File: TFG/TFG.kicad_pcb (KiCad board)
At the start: 2 copper layers, 68.3 x 67.9 mm, 36 parts, among them IC1 MC74VHC1GT14DBVT1G, IC2 AMS1117-5.0, IC3 AMS1117-5.0, J1 Jack-DC, J2 CON-SMA-EDGE-SRP, J3 CON-SMA-EDGE-SRP, Q1 BFP420

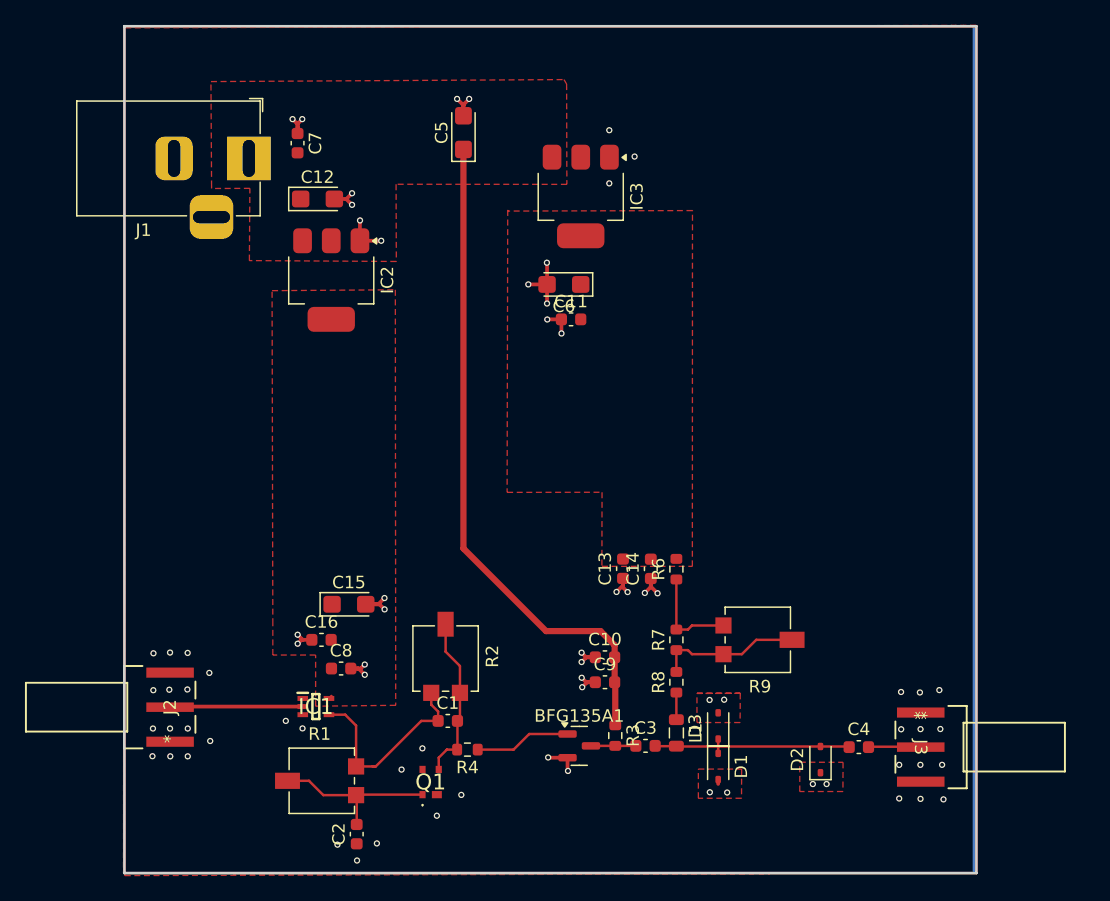
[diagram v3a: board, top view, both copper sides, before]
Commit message: Updated Schottky and SRD diodes in PCB and BOM, everything is ready to check, only DRC is missing
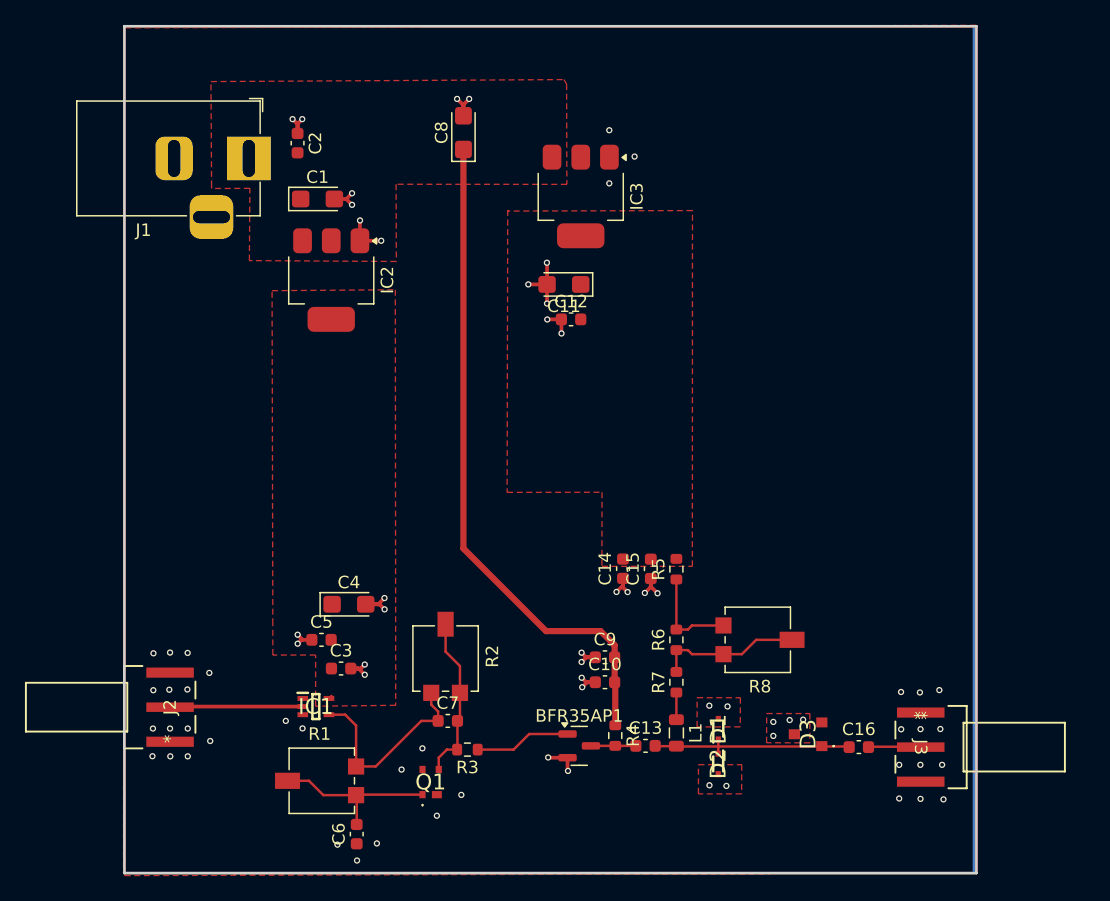
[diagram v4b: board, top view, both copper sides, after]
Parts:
- removed the D2 at (91.7, 75.4)
- added D3: SRD_MA144769-287T, MA144769-287T:MA144769287T, F.Cu at (90.7, 73.4)
- D1: renamed from D3; value D_Schottky_BAT15 -> SMS3923-079LF; footprint Diode_SMD:D_SOD-323 -> SMS3923-079LF:SODFL1608X70N
- D2: renamed from D1; value D_Schottky_BAT15 -> SMS3923-079LF; footprint Diode_SMD:D_SOD-323 -> SMS3923-079LF:SODFL1608X70N
- IC1: value MC74VHC1GT14DBVT1G -> MC74VHC1GT04DFT2G
- IC2, IC3: value AMS1117-5.0 -> TS1117BCW50 RPG
- moved D1 0.27 mm to (83.5, 73.0)
- moved D2 0.20 mm to (83.5, 75.7)
- renumbered BFG135A1 to BFR35AP1, C12 to C1, C9 to C10, C6 to C11, C11 to C12, C3 to C13, C13 to C14, C14 to C15, C4 to C16, C7 to C2, C8 to C3, C15 to C4, C16 to C5, C2 to C6, C1 to C7, C5 to C8, C10 to C9, R4 to R3, R3 to R4, R6 to R5, R7 to R6, R8 to R7, R9 to R8
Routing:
- net GND: track 38.1 -> 37.7 mm, vias 73 -> 75

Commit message: Final design for Ultrawideband pulse generator PCB - v1
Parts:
- added REF**: MountingHole_2mm, MountingHole:MountingHole_2mm, F.Cu at (50.9, 75.8)
- added REF**: MountingHole_2mm, MountingHole:MountingHole_2mm, F.Cu at (50.9, 34.1)
- added REF**: MountingHole_2mm, MountingHole:MountingHole_2mm, F.Cu at (99.6, 34.1)
- added REF**: MountingHole_2mm, MountingHole:MountingHole_2mm, F.Cu at (99.6, 75.8)
- moved C8 28.5 mm to (65.5, 53.5), turned to -90 degrees
- moved C2 21.0 mm to (61.3, 43.6), turned to 180 degrees
- moved C1 20.2 mm to (61.2, 48.1)
- moved IC3 19.5 mm to (74.0, 49.7), turned to 0 degrees
- moved J1 18.2 mm to (55.9, 42.4)
- moved IC2 17.9 mm to (56.7, 54.3), turned to 180 degrees
- moved C6 17.4 mm to (69.5, 72.5)
- moved C11 16.9 mm to (81.1, 51.0), turned to -90 degrees
- moved C12 16.0 mm to (83.9, 50.5), turned to 90 degrees
- moved C14 15.5 mm to (89.2, 52.2), turned to 180 degrees
- moved C15 15.0 mm to (89.2, 50.0), turned to 180 degrees
- moved R1 14.6 mm to (65.5, 72.5), turned to 90 degrees
- moved Q1 14.0 mm to (71.0, 68.0)
- moved R3 13.6 mm to (72.5, 64.5)
- moved J2 10.1 mm to (47.9, 66.8)
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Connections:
- J1 pad 3: (no net) -> GND
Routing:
- net /V12v: track 54.0 -> 0.57 mm
- net GND: track 37.7 -> 0.32 mm, vias 75 -> 116
- net Net-(IC1-Y): track 16.4 -> 9.75 mm
- net Net-(BFR35AP1-B): track 7.57 -> 4.04 mm
- net Net-(Q1-C): track 13.5 -> 16.2 mm
- net /Vout: track 5.46 -> 3.08 mm
- net Net-(R5-Pad1): track 7.95 -> 6.44 mm
- net /V3v_in: track 10.5 -> 9.27 mm
- net /V5v: track 1.05 -> 0.00 mm
- net Net-(Q1-B): track 13.7 -> 12.8 mm
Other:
- board size 68.3 x 67.9 mm -> 56.7 x 48.9 mm

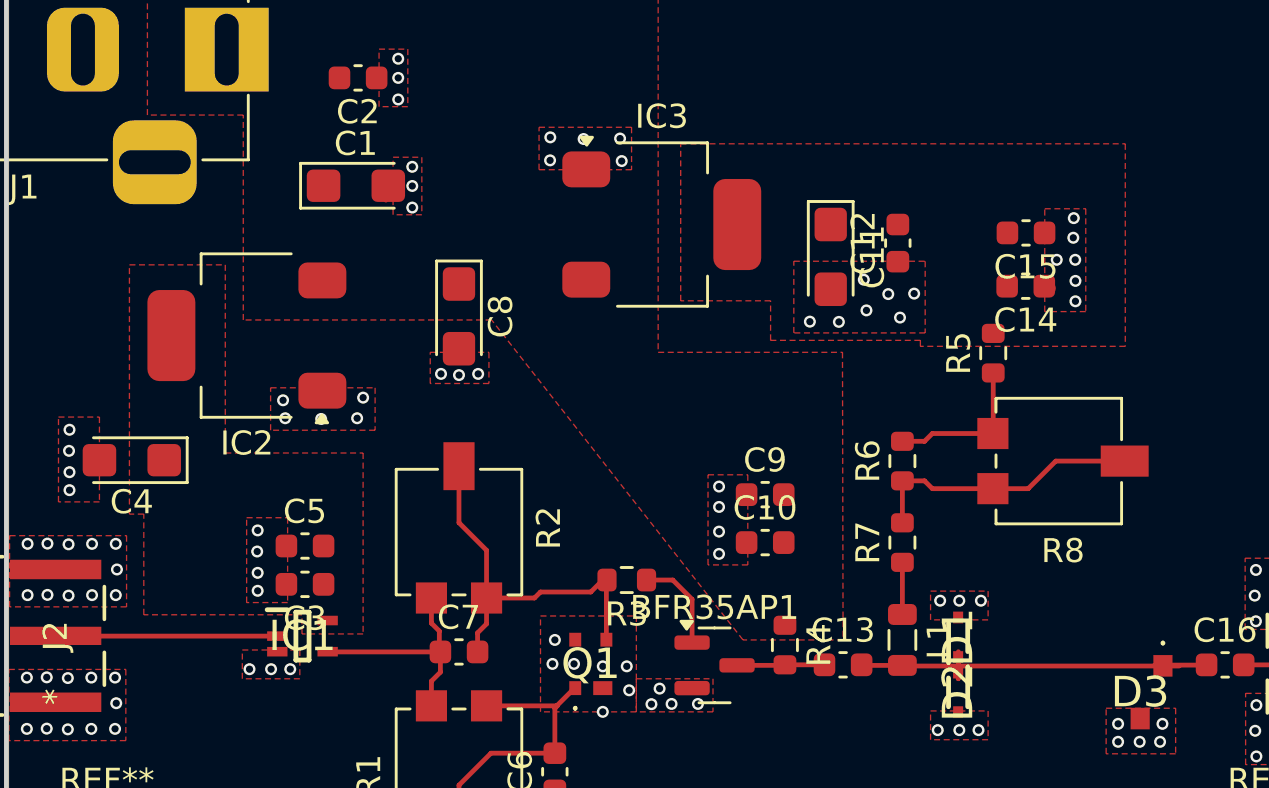
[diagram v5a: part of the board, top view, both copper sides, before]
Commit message: Final design for Ultrawideband pulse generator PCB, corrected some missing thermal spokes - v2
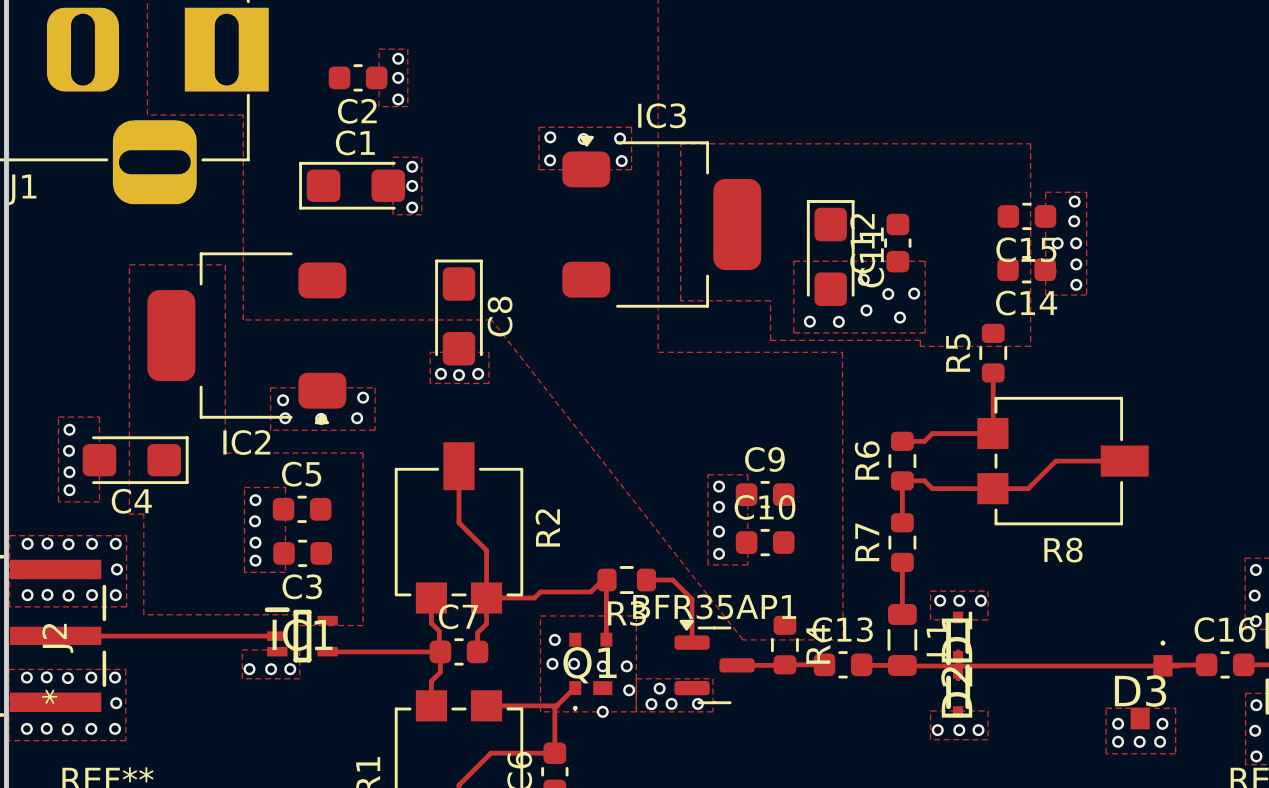
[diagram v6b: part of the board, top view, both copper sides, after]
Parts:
- moved C5 1.53 mm to (59.0, 61.6)
- moved C3 1.29 mm to (59.0, 63.4)
- moved C14 0.69 mm to (89.2, 51.6)
- moved C15 0.69 mm to (89.2, 49.3)

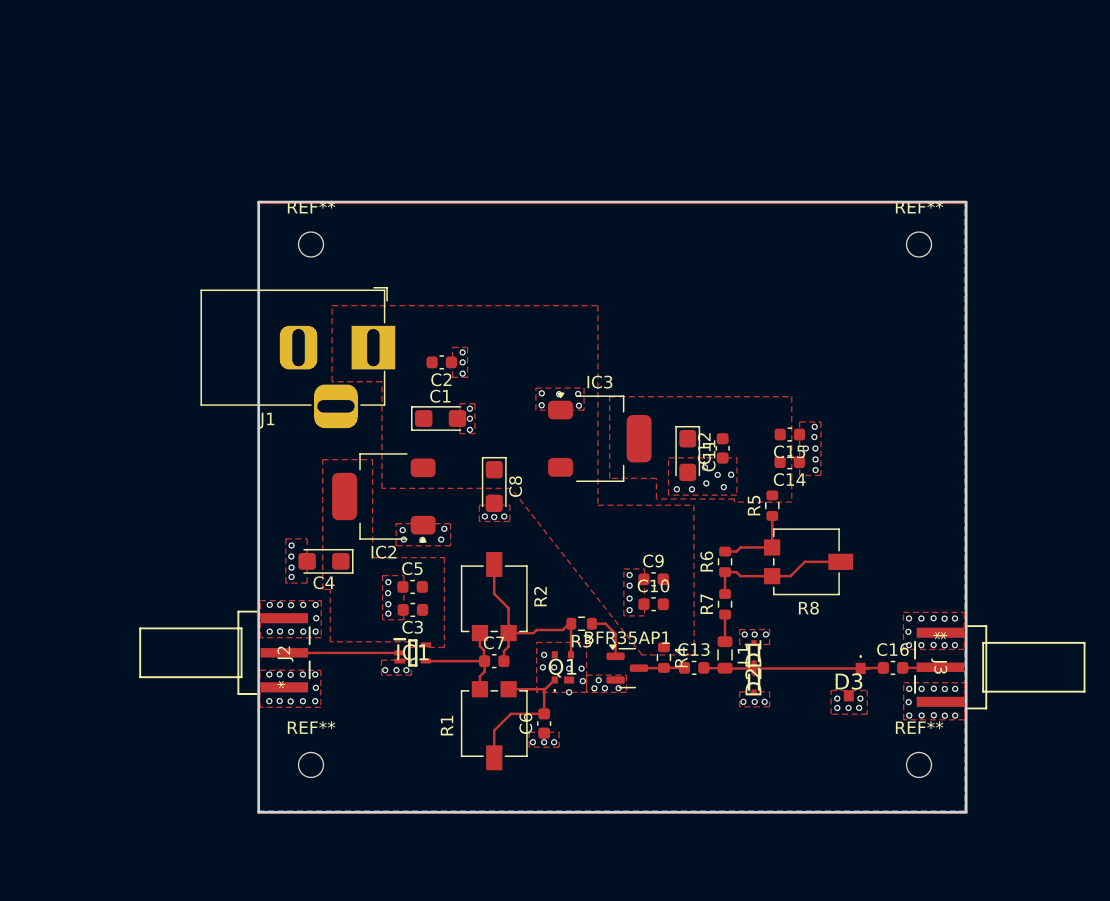
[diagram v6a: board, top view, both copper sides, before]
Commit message: Final version v1 with Zo=90 ohms in delay line
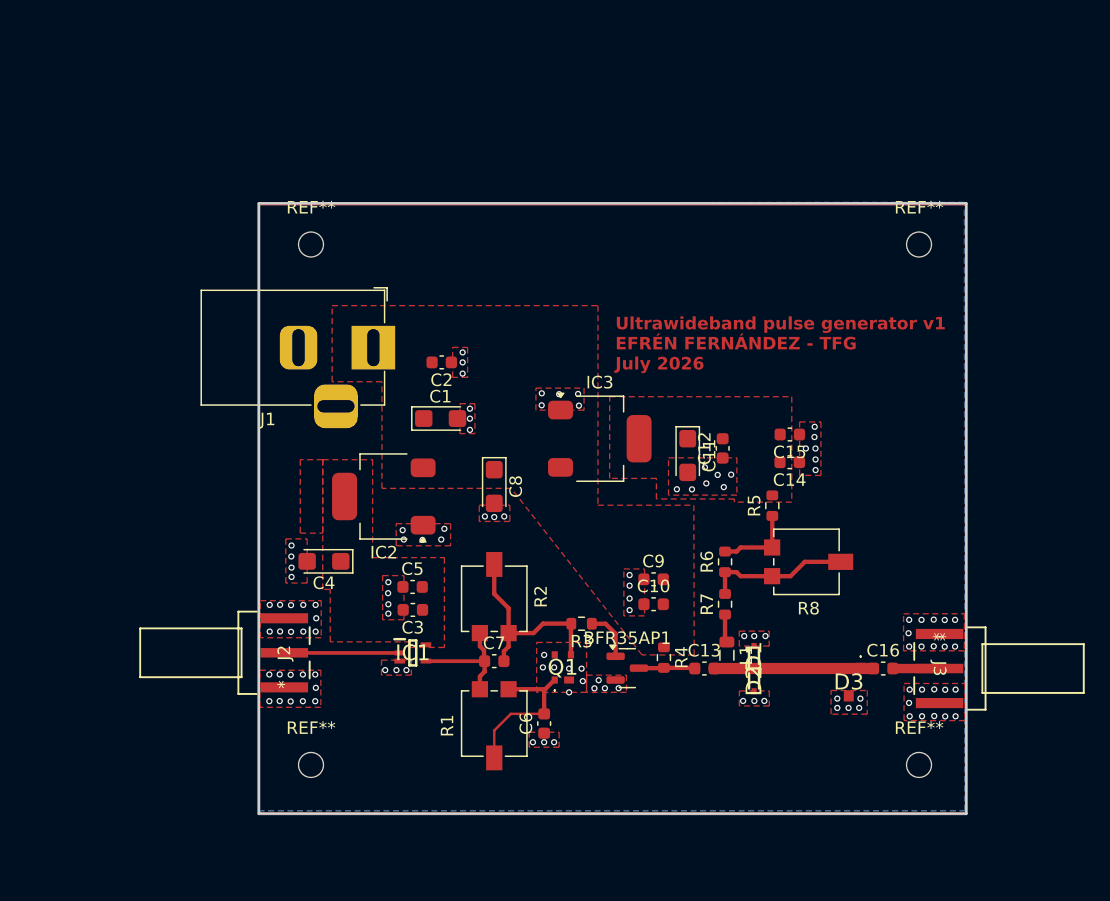
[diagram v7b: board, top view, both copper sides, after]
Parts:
- moved C13 0.83 mm to (82.4, 68.1)
- moved C16 0.79 mm to (96.7, 68.1)
- moved D1 0.23 mm to (86.4, 67.1)
- moved L1 0.15 mm to (84.2, 67.0)
- moved J3 0.12 mm to (102.1, 68.1)
- moved D2 0.10 mm to (86.4, 69.1)
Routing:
- net Net-(D1-K): track 16.8 -> 12.7 mm
- net /Vout_Driver: track 3.66 -> 4.51 mm
- net /Vout: track 3.08 -> 3.81 mm
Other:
- board text added: "Ultrawideband pulse generator v1 EFRÉN FERNÁNDEZ - TFG July 2026"
